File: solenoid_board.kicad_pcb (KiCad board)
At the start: 2 copper layers, 29 parts, among them J1 Screw_Terminal_01x02, J10 Screw_Terminal_01x02, J11 Screw_Terminal_01x02, J2 MCU_LEFT_LEGS, J3 MCU_RIGHT_LEGS, J4 Solenoid_PWR_Supply, J5 RJ45, J6 Screw_Terminal_01x06, J7 Screw_Terminal_01x02, J8 Screw_Terminal_01x02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

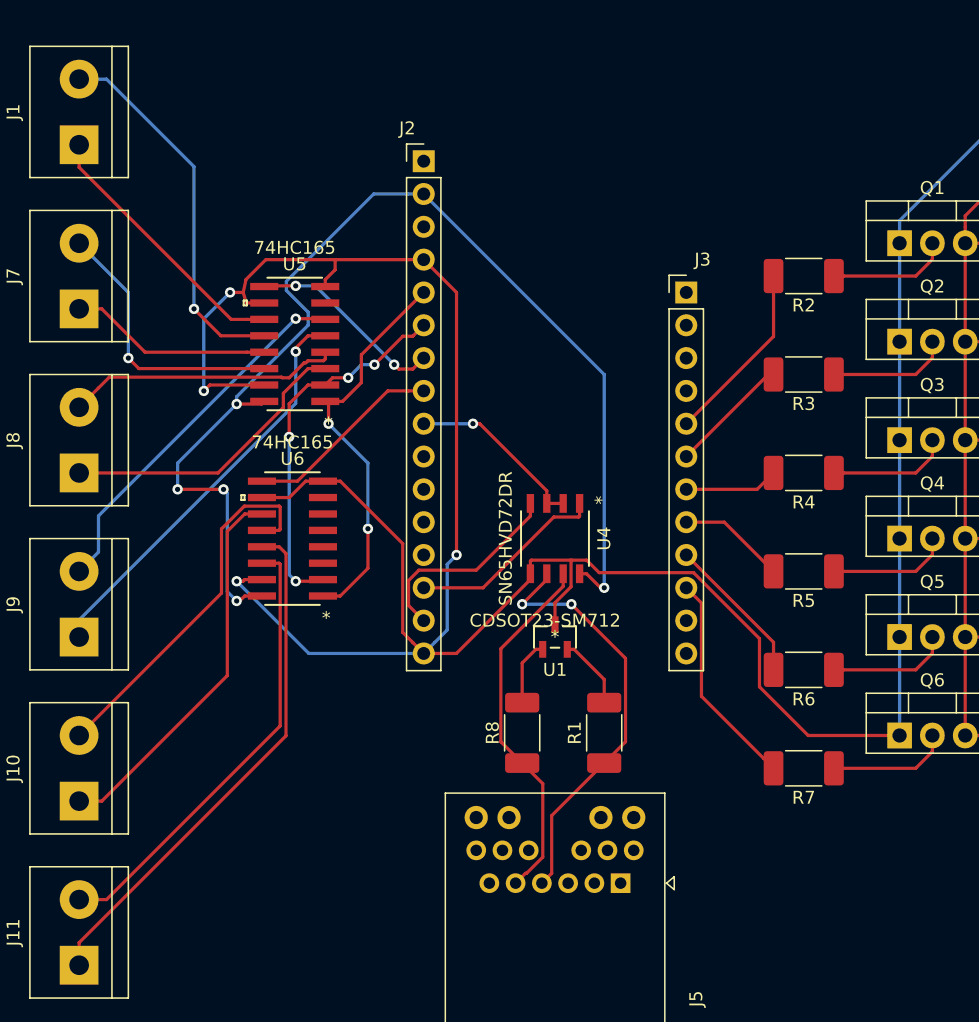
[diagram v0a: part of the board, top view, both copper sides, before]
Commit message: update schematic and netlist, fixing traces
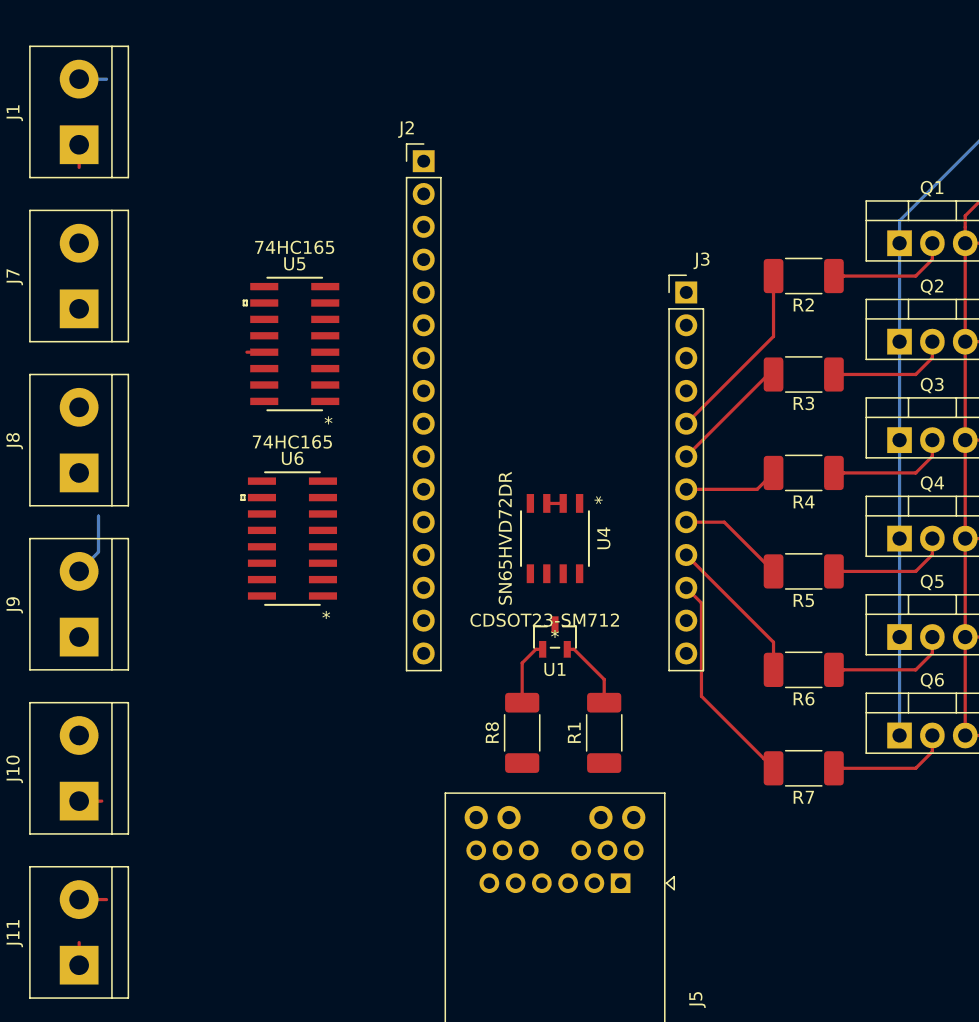
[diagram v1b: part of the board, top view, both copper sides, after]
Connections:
- U5 pad 10: GND -> /SHIFT2_OUT
- U5 pad 2: /A1 -> /SCK
- U5 pad 9: /A2 -> /MISO
- U6 pad 2: /A1 -> /SCK
- U6 pad 9: /A3 -> /SHIFT2_OUT
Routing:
- net GND: track 223.0 -> 60.7 mm, vias 4 -> 0
- net /3V3: track 90.0 -> 0.00 mm, vias 5 -> 0
- net /INP5_0: track 40.6 -> 1.75 mm
- net /INP5_1: track 35.1 -> 2.12 mm
- net /RJ45_4: track 33.0 -> 0.00 mm, vias 2 -> 0
- net /A0: track 31.0 -> 0.00 mm, vias 2 -> 0
- net /INP3_0: track 32.0 -> 1.33 mm, vias 1 -> 0
- net /A1: track 29.0 -> 0.00 mm, vias 4 -> 0
- net /INP4_1: track 29.0 -> 0.00 mm
- net /RJ45_5: track 28.2 -> 0.00 mm
- net /INP4_0: track 29.9 -> 1.75 mm
- net /INP0_1: track 29.0 -> 2.12 mm, vias 1 -> 0
- net /INP3_1: track 28.8 -> 4.92 mm, vias 1 -> 0
- net /INP2_0: track 23.0 -> 0.00 mm
- net /INP1_1: track 21.3 -> 0.00 mm, vias 1 -> 0
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
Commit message: Finish routing
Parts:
- added J12: Screw_Terminal_01x06, TerminalBlock:TerminalBlock_bornier-6_P5.08mm, F.Cu at (183.4, 102.1)
- moved J6 9.52 mm to (183.4, 70.1)
- moved J11 5.84 mm to (103.1, 121.9), turned to 270 degrees
- moved J10 5.33 mm to (103.1, 109.7), turned to 270 degrees
- moved J9 4.83 mm to (103.1, 97.5), turned to 270 degrees
- moved J8 4.32 mm to (103.1, 85.3), turned to 270 degrees
- moved J1 4.32 mm to (103.1, 59.9), turned to 270 degrees
- moved J7 4.32 mm to (103.1, 72.6), turned to 270 degrees
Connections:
- J6 pad 2: +48V -> Net-(J6-Pad2)
- J6 pad 4: +48V -> Net-(J6-Pad4)
- J6 pad 6: +48V -> Net-(J6-Pad6)
- Q1 pad 3: +48V -> Net-(J6-Pad2)
- Q2 pad 3: +48V -> Net-(J6-Pad4)
- Q3 pad 3: +48V -> Net-(J6-Pad6)
- Q4 pad 3: +48V -> Net-(J12-Pad2)
- Q5 pad 3: +48V -> Net-(J12-Pad4)
- Q6 pad 3: +48V -> Net-(J12-Pad6)
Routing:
- net /3V3: track 0.00 -> 97.5 mm, vias 0 -> 3
- net /SCK: track 0.00 -> 49.1 mm
- net +48V: track 125.2 -> 80.5 mm
- net GND: track 60.7 -> 18.4 mm, vias 0 -> 6
- net /INP3_1: track 4.92 -> 40.6 mm, vias 0 -> 2
- net /RJ45_5: track 0.00 -> 35.4 mm
- net /INP5_1: track 2.12 -> 37.0 mm
- net /MISO: track 0.00 -> 33.8 mm, vias 0 -> 2
- net /RJ45_4: track 0.00 -> 33.4 mm
- net /INP5_0: track 1.75 -> 34.2 mm
- net /INP3_0: track 1.33 -> 33.7 mm, vias 0 -> 2
- net /A0: track 0.00 -> 32.1 mm
- net /INP2_1: track 0.00 -> 30.0 mm, vias 0 -> 2
- net /INP4_1: track 0.00 -> 27.5 mm
- net /INP2_0: track 0.00 -> 27.3 mm, vias 0 -> 2
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- added copper zone on B.Cu, net GND
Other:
- board outline added: 90.9 x 93 mm
- net class HV added: clearance 0.2, trace_width 0.508, via_dia 0.8, via_drill 0.4

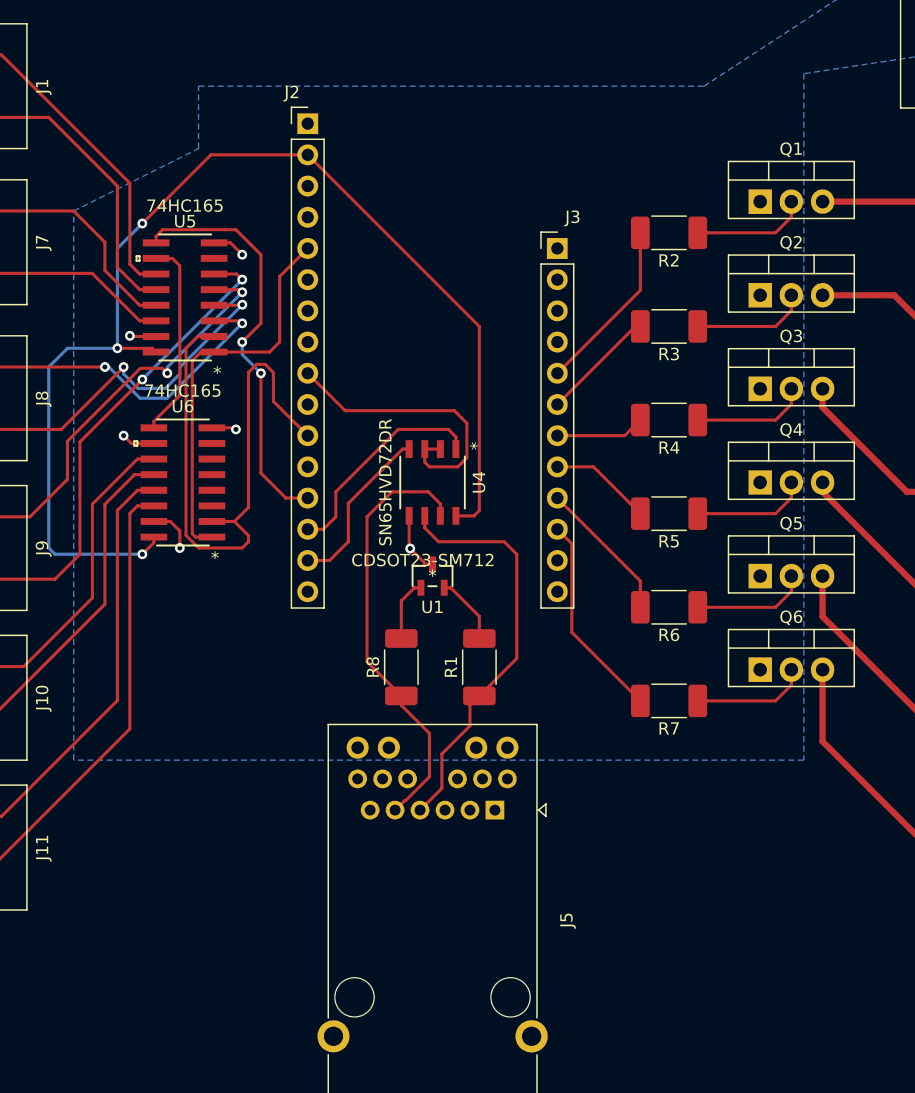
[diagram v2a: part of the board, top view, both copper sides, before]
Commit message: Add grounding pin
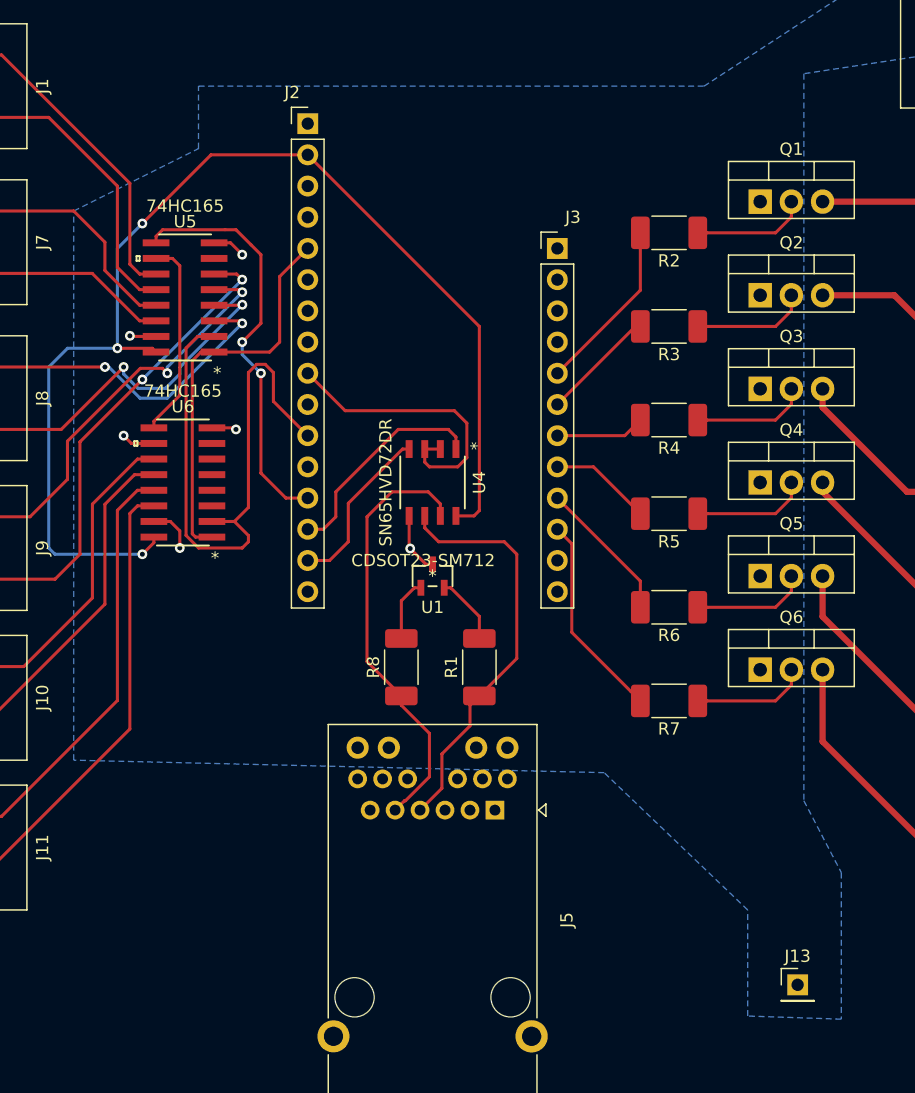
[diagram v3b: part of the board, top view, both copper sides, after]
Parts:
- added J13: Conn_01x01_Male, Connector_PinHeader_2.54mm:PinHeader_1x01_P2.54mm_Vertical, F.Cu at (169.7, 135.6)
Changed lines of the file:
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@@
     (tracks 291)
     (zones 0)
-    (modules 30)
+    (modules 31)
     (nets 70)
   )
@@
     (add_net "Net-(J6-Pad4)")
     (add_net "Net-(J6-Pad6)")
+  )
+  (module Connector_PinHeader_2.54mm:PinHeader_1x01_P2.54mm_Vertical (layer F.Cu)
+    (at 169.672 135.636)
+    (descr "Through hole straight pin header, 1x01, 2.54mm pitch, single row")
+    (tags "Through hole pin header THT 1x01 2.54mm single row")
+    (fp_text reference J13 (at 0 -2.33) (layer F.SilkS)
+      (effects (font (size 1 1) (thickness 0.15)))
+    )
+    (fp_text value Conn_01x01_Male (at 0 2.33) (layer F.Fab)
+      (effects (font (size 1 1) (thickness 0.15)))
+    )
+    (fp_text user %R (at 0 0 90) (layer F.Fab)
+      (effects (font (size 1 1) (thickness 0.15)))
+    )
+    (fp_line (start 1.8 -1.8) (end -1.8 -1.8) (layer F.CrtYd) (width 0.05))
+    (fp_line (start 1.8 1.8) (end 1.8 -1.8) (layer F.CrtYd) (width 0.05))
+    (fp_line (start -1.8 1.8) (end 1.8 1.8) (layer F.CrtYd) (width 0.05))
+    (fp_line (start -1.8 -1.8) (end -1.8 1.8) (layer F.CrtYd) (width 0.05))
+    (fp_line (start -1.33 -1.33) (end 0 -1.33) (layer F.SilkS) (width 0.12))
+    (fp_line (start -1.33 0) (end -1.33 -1.33) (layer F.SilkS) (width 0.12))
+    (fp_line (start -1.33 1.27) (end 1.33 1.27) (layer F.SilkS) (width 0.12))
+    (fp_line (start 1.33 1.27) (end 1.33 1.33) (layer F.SilkS) (width 0.12))
+    (fp_line (start -1.33 1.27) (end -1.33 1.33) (layer F.SilkS) (width 0.12))
+    (fp_line (start -1.33 1.33) (end 1.33 1.33) (layer F.SilkS) (width 0.12))
+    (fp_line (start -1.27 -0.635) (end -0.635 -1.27) (layer F.Fab) (width 0.1))
+    (fp_line (start -1.27 1.27) (end -1.27 -0.635) (layer F.Fab) (width 0.1))
+    (fp_line (start 1.27 1.27) (end -1.27 1.27) (layer F.Fab) (width 0.1))
+    (fp_line (start 1.27 -1.27) (end 1.27 1.27) (layer F.Fab) (width 0.1))
+    (fp_line (start -0.635 -1.27) (end 1.27 -1.27) (layer F.Fab) (width 0.1))
+    (pad 1 thru_hole rect (at 0 0) (size 1.7 1.7) (drill 1) (layers *.Cu *.Mask)
+      (net 13 GND))
+    (model ${KISYS3DMOD}/Connector_PinHeader_2.54mm.3dshapes/PinHeader_1x01_P2.54mm_Vertical.wrl
+      (at (xyz 0 0 0))
+      (scale (xyz 1 1 1))
+      (rotate (xyz 0 0 0))
+    )
   )
   (module TerminalBlock:TerminalBlock_bornier-6_P5.08mm (layer F.Cu)
@@
     (polygon
       (pts
-        (xy 186.944 58.928) (xy 170.18 61.468) (xy 170.18 117.348) (xy 110.744 117.348) (xy 110.744 72.644)
+        (xy 186.944 58.928) (xy 170.18 61.468) (xy 170.18 120.65) (xy 173.228 126.492) (xy 173.228 138.43)
+        (xy 165.608 138.176) (xy 165.608 129.54) (xy 153.924 118.364) (xy 110.744 117.348) (xy 110.744 72.644)
         (xy 120.904 67.564) (xy 120.904 62.484) (xy 162.052 62.484) (xy 175.26 53.848) (xy 186.944 53.848)
       )

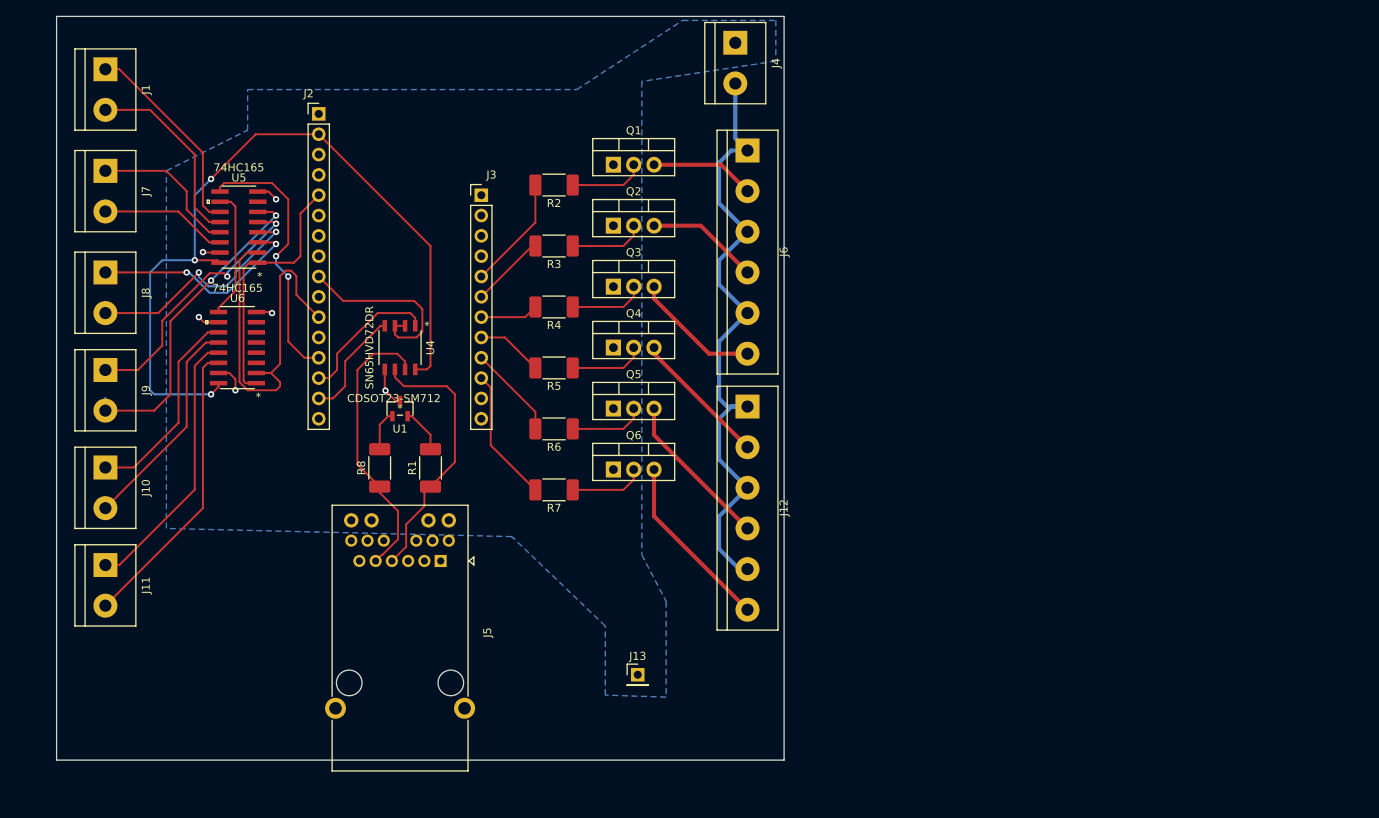
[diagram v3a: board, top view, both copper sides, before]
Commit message: Added a +5V Supply input and connected it to the Feather board. Added a second RJ45 port, and connected the 4th and 5th wires of both RJ45 ports together. Added 4 capacitors to maintain a voltage on the supply pins of the digital electronics, and picked out the footprints. Added a +3V3 terminal block, to power the solenoid switches. Changed the supply voltage to the 8-bit shifters from +3V3 to +5V, as is typical according to the datasheet. Still need to clean up the schematic, add a BOM, change the footprint of the large electrolytic capacitor to a smaller size, finalize the geometry of the PCB layout, generate the gerber files, and order the sucker.
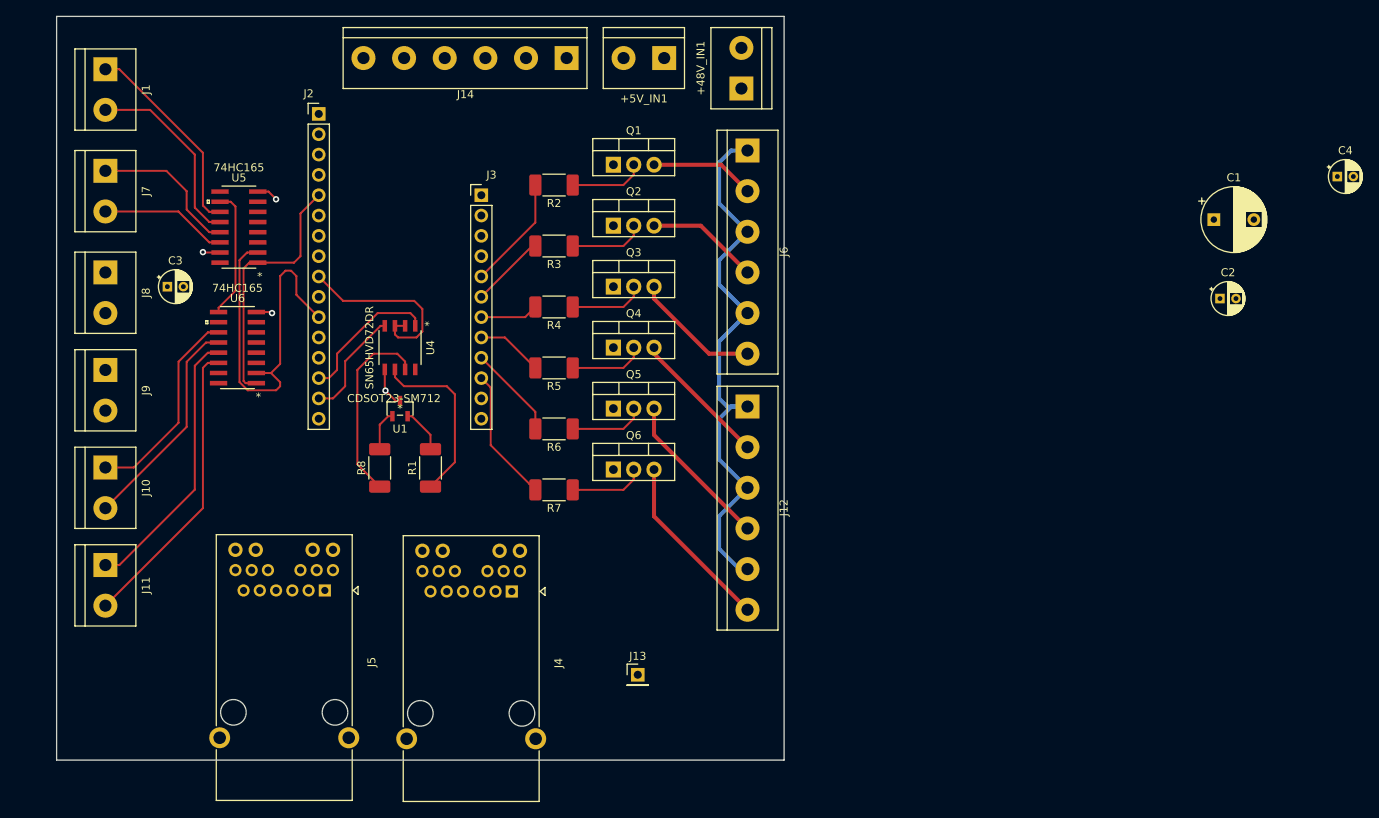
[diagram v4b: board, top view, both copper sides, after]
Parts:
- added +5V_IN1: MCU_PWR_Supply, TerminalBlock:TerminalBlock_bornier-2_P5.08mm, F.Cu at (173.0, 58.5)
- added C1: CP, Capacitor_THT:CP_Radial_D8.0mm_P5.00mm, F.Cu at (241.7, 78.7)
- added C2: 0.1 nF, Capacitor_THT:CP_Radial_D4.0mm_P2.00mm, F.Cu at (242.4, 88.6)
- added C3: 0.1 nF, Capacitor_THT:CP_Radial_D4.0mm_P2.00mm, F.Cu at (110.9, 87.1)
- added C4: 0.1 nF, Capacitor_THT:CP_Radial_D4.0mm_P2.00mm, F.Cu at (257.1, 73.4)
- added J14: Screw_Terminal_01x06, TerminalBlock:TerminalBlock_bornier-6_P5.08mm, F.Cu at (160.8, 58.5)
- added J4: RJ45, Connector_RJ:RJ45_Pulse_JK0654219NL_Horizontal, F.Cu at (153.9, 125.2)
- moved J5 14.9 mm to (130.6, 125.1)
- moved +48V_IN1 5.77 mm to (182.6, 62.4), turned to 90 degrees
- renumbered J4 to +48V_IN1
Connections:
- J2 pad 1: /RST -> (no net)
- J2 pad 10: /A5 -> (no net)
- J2 pad 12: /MOSI -> (no net)
- J2 pad 2: /3V3 -> +3V3
- J2 pad 3: /ARf -> (no net)
- J2 pad 6: /A1 -> (no net)
- J2 pad 7: /A2 -> (no net)
- J2 pad 8: /A3 -> (no net)
- J3 pad 1: /BAT -> (no net)
- J3 pad 11: /SCL -> (no net)
- J3 pad 12: /SDA -> (no net)
- J3 pad 2: /En -> (no net)
- J3 pad 3: /USB -> +5V
- J3 pad 4: /D13 -> (no net)
- J5 pad 1: Net-(J5-Pad1) -> (no net)
- J5 pad 2: Net-(J5-Pad2) -> (no net)
- J5 pad 3: Net-(J5-Pad3) -> (no net)
- J5 pad 6: Net-(J5-Pad6) -> (no net)
- J5 pad 7: Net-(J5-Pad7) -> (no net)
- J5 pad 8: Net-(J5-Pad8) -> (no net)
- U4 pad 8: /3V3 -> +3V3
- U5 pad 16: /3V3 -> +5V
- U5 pad 7: Net-(U5-Pad7) -> (no net)
- U6 pad 16: /3V3 -> +5V
- U6 pad 3: Net-(U6-Pad3) -> (no net)
- U6 pad 4: Net-(U6-Pad4) -> (no net)
- U6 pad 5: Net-(U6-Pad5) -> (no net)
- U6 pad 6: Net-(U6-Pad6) -> (no net)
- U6 pad 7: Net-(U6-Pad7) -> (no net)
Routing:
- net /3V3: track 97.5 -> 0.00 mm, vias 3 -> 0
- net /INP3_1: track 40.6 -> 0.00 mm, vias 2 -> 0
- net /MISO: track 33.8 -> 0.00 mm, vias 2 -> 0
- net /INP3_0: track 33.7 -> 0.00 mm, vias 2 -> 0
- net /INP2_1: track 30.0 -> 0.00 mm, vias 2 -> 0
- net /INP2_0: track 27.3 -> 0.00 mm, vias 2 -> 0
- net /RJ45_5: track 35.4 -> 23.9 mm
- net /RJ45_4: track 33.4 -> 22.2 mm
- net +48V: track 80.5 -> 71.5 mm
- net GND: track 18.4 -> 11.9 mm, vias 6 -> 4
- removed copper zone on B.Cu, net GND
